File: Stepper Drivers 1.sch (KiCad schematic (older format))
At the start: 88 parts, among them J3 Conn_01x04, J4 Conn_01x04, J5 Conn_01x04, J6 Conn_01x04

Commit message: associated more footprints
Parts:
- C102, C103, C104, C105, C106, C107, C108, C109, C59, C61, C74, C75, C76, C77, C78, C79, C80, C81, C87, C89: footprint (none) -> Capacitor_SMD:C_0603_1608Metric_Pad1.05x0.95mm_HandSolder
- C56, C57, C84, C85: footprint (none) -> Capacitor_SMD:C_0805_2012Metric_Pad1.15x1.40mm_HandSolder
- J3, J4, J5, J6: footprint (none) -> Connector_Molex:Molex_KK-254_AE-6410-04A_1x04_P2.54mm_Vertical
- JP10, JP11, JP6, JP7: footprint (none) -> Connector_PinHeader_2.54mm:PinHeader_1x03_P2.54mm_Vertical
- JP4, JP5, JP8, JP9: footprint (none) -> Connector_PinHeader_2.54mm:PinHeader_1x02_P2.54mm_Vertical
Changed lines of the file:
@@
 F 0 "C61" V 3542 1696 39  0000 L BNN
 F 1 "22nF" V 3542 1605 39  0000 R BNN
-F 2 "" H 3450 1650 50  0001 C CNN
+F 2 "Capacitor_SMD:C_0603_1608Metric_Pad1.05x0.95mm_HandSolder" H 3450 1650 50  0001 C CNN
 F 3 "~" H 3450 1650 50  0001 C CNN
 	1    3450 1650
@@
 F 0 "C57" V 1942 1346 39  0000 L BNN
 F 1 "4.7uF" V 1942 1255 39  0000 R BNN
-F 2 "" H 1850 1300 50  0001 C CNN
+F 2 "Capacitor_SMD:C_0805_2012Metric_Pad1.15x1.40mm_HandSolder" H 1850 1300 50  0001 C CNN
 F 3 "~" H 1850 1300 50  0001 C CNN
 	1    1850 1300
@@
 F 0 "JP5" H 1550 1850 39  0000 R BNN
 F 1 "Stall Detection" H 1650 1900 39  0000 L TNN
-F 2 "" H 1600 1800 50  0001 C CNN
+F 2 "Connector_PinHeader_2.54mm:PinHeader_1x02_P2.54mm_Vertical" H 1600 1800 50  0001 C CNN
 F 3 "~" H 1600 1800 50  0001 C CNN
 	1    1600 1800
@@
 F 0 "C75" V 4542 2296 39  0000 L BNN
 F 1 "1nF" V 4542 2205 39  0000 R BNN
-F 2 "" H 4450 2250 50  0001 C CNN
+F 2 "Capacitor_SMD:C_0603_1608Metric_Pad1.05x0.95mm_HandSolder" H 4450 2250 50  0001 C CNN
 F 3 "~" H 4450 2250 50  0001 C CNN
 	1    4450 2250
@@
 F 0 "C77" V 4692 2296 39  0000 L BNN
 F 1 "1nF" V 4692 2205 39  0000 R BNN
-F 2 "" H 4600 2250 50  0001 C CNN
+F 2 "Capacitor_SMD:C_0603_1608Metric_Pad1.05x0.95mm_HandSolder" H 4600 2250 50  0001 C CNN
 F 3 "~" H 4600 2250 50  0001 C CNN
 	1    4600 2250
@@
 F 0 "C79" V 4842 2296 39  0000 L BNN
 F 1 "1nF" V 4842 2205 39  0000 R BNN
-F 2 "" H 4750 2250 50  0001 C CNN
+F 2 "Capacitor_SMD:C_0603_1608Metric_Pad1.05x0.95mm_HandSolder" H 4750 2250 50  0001 C CNN
 F 3 "~" H 4750 2250 50  0001 C CNN
 	1    4750 2250
@@
 F 0 "C81" V 4992 2296 39  0000 L BNN
 F 1 "1nF" V 4992 2205 39  0000 R BNN
-F 2 "" H 4900 2250 50  0001 C CNN
+F 2 "Capacitor_SMD:C_0603_1608Metric_Pad1.05x0.95mm_HandSolder" H 4900 2250 50  0001 C CNN
 F 3 "~" H 4900 2250 50  0001 C CNN
 	1    4900 2250
@@
 F 0 "J4" H 5280 1292 50  0000 L CNN
 F 1 "Conn_01x04" H 5280 1201 50  0000 L CNN
-F 2 "" H 5200 1300 50  0001 C CNN
+F 2 "Connector_Molex:Molex_KK-254_AE-6410-04A_1x04_P2.54mm_Vertical" H 5200 1300 50  0001 C CNN
 F 3 "~" H 5200 1300 50  0001 C CNN
 	1    5200 1300
@@
 F 0 "C87" V 8892 1696 39  0000 L BNN
 F 1 "22nF" V 8892 1605 39  0000 R BNN
-F 2 "" H 8800 1650 50  0001 C CNN
+F 2 "Capacitor_SMD:C_0603_1608Metric_Pad1.05x0.95mm_HandSolder" H 8800 1650 50  0001 C CNN
 F 3 "~" H 8800 1650 50  0001 C CNN
 	1    8800 1650
@@
 F 0 "C84" V 7292 1346 39  0000 L BNN
 F 1 "4.7uF" V 7292 1255 39  0000 R BNN
-F 2 "" H 7200 1300 50  0001 C CNN
+F 2 "Capacitor_SMD:C_0805_2012Metric_Pad1.15x1.40mm_HandSolder" H 7200 1300 50  0001 C CNN
 F 3 "~" H 7200 1300 50  0001 C CNN
 	1    7200 1300
@@
 F 0 "JP8" H 6900 1850 39  0000 R BNN
 F 1 "Stall Detection" H 7000 1900 39  0000 L TNN
-F 2 "" H 6950 1800 50  0001 C CNN
+F 2 "Connector_PinHeader_2.54mm:PinHeader_1x02_P2.54mm_Vertical" H 6950 1800 50  0001 C CNN
 F 3 "~" H 6950 1800 50  0001 C CNN
 	1    6950 1800
@@
 F 0 "C102" V 9892 2296 39  0000 L BNN
 F 1 "1nF" V 9892 2205 39  0000 R BNN
-F 2 "" H 9800 2250 50  0001 C CNN
+F 2 "Capacitor_SMD:C_0603_1608Metric_Pad1.05x0.95mm_HandSolder" H 9800 2250 50  0001 C CNN
 F 3 "~" H 9800 2250 50  0001 C CNN
 	1    9800 2250
@@
 F 0 "C104" V 10042 2296 39  0000 L BNN
 F 1 "1nF" V 10042 2205 39  0000 R BNN
-F 2 "" H 9950 2250 50  0001 C CNN
+F 2 "Capacitor_SMD:C_0603_1608Metric_Pad1.05x0.95mm_HandSolder" H 9950 2250 50  0001 C CNN
 F 3 "~" H 9950 2250 50  0001 C CNN
 	1    9950 2250
@@
 F 0 "C106" V 10192 2296 39  0000 L BNN
 F 1 "1nF" V 10192 2205 39  0000 R BNN
-F 2 "" H 10100 2250 50  0001 C CNN
+F 2 "Capacitor_SMD:C_0603_1608Metric_Pad1.05x0.95mm_HandSolder" H 10100 2250 50  0001 C CNN
 F 3 "~" H 10100 2250 50  0001 C CNN
 	1    10100 2250
@@
 F 0 "C108" V 10342 2296 39  0000 L BNN
 F 1 "1nF" V 10342 2205 39  0000 R BNN
-F 2 "" H 10250 2250 50  0001 C CNN
+F 2 "Capacitor_SMD:C_0603_1608Metric_Pad1.05x0.95mm_HandSolder" H 10250 2250 50  0001 C CNN
 F 3 "~" H 10250 2250 50  0001 C CNN
 	1    10250 2250
@@
 F 0 "J5" H 10630 1292 50  0000 L CNN
 F 1 "Conn_01x04" H 10630 1201 50  0000 L CNN
-F 2 "" H 10550 1300 50  0001 C CNN
+F 2 "Connector_Molex:Molex_KK-254_AE-6410-04A_1x04_P2.54mm_Vertical" H 10550 1300 50  0001 C CNN
 F 3 "~" H 10550 1300 50  0001 C CNN
 	1    10550 1300
@@
 F 0 "C59" V 3492 4646 39  0000 L BNN
 F 1 "22nF" V 3492 4555 39  0000 R BNN
-F 2 "" H 3400 4600 50  0001 C CNN
+F 2 "Capacitor_SMD:C_0603_1608Metric_Pad1.05x0.95mm_HandSolder" H 3400 4600 50  0001 C CNN
 F 3 "~" H 3400 4600 50  0001 C CNN
 	1    3400 4600
@@
 F 0 "C56" V 1892 4296 39  0000 L BNN
 F 1 "4.7uF" V 1892 4205 39  0000 R BNN
-F 2 "" H 1800 4250 50  0001 C CNN
+F 2 "Capacitor_SMD:C_0805_2012Metric_Pad1.15x1.40mm_HandSolder" H 1800 4250 50  0001 C CNN
 F 3 "~" H 1800 4250 50  0001 C CNN
 	1    1800 4250
@@
 F 0 "JP4" H 1500 4800 39  0000 R BNN
 F 1 "Stall Detection" H 1600 4850 39  0000 L TNN
-F 2 "" H 1550 4750 50  0001 C CNN
+F 2 "Connector_PinHeader_2.54mm:PinHeader_1x02_P2.54mm_Vertical" H 1550 4750 50  0001 C CNN
 F 3 "~" H 1550 4750 50  0001 C CNN
 	1    1550 4750
@@
 F 0 "C74" V 4492 5246 39  0000 L BNN
 F 1 "1nF" V 4492 5155 39  0000 R BNN
-F 2 "" H 4400 5200 50  0001 C CNN
+F 2 "Capacitor_SMD:C_0603_1608Metric_Pad1.05x0.95mm_HandSolder" H 4400 5200 50  0001 C CNN
 F 3 "~" H 4400 5200 50  0001 C CNN
 	1    4400 5200
@@
 F 0 "C76" V 4642 5246 39  0000 L BNN
 F 1 "1nF" V 4642 5155 39  0000 R BNN
-F 2 "" H 4550 5200 50  0001 C CNN
+F 2 "Capacitor_SMD:C_0603_1608Metric_Pad1.05x0.95mm_HandSolder" H 4550 5200 50  0001 C CNN
 F 3 "~" H 4550 5200 50  0001 C CNN
 	1    4550 5200
@@
 F 0 "C78" V 4792 5246 39  0000 L BNN
 F 1 "1nF" V 4792 5155 39  0000 R BNN
-F 2 "" H 4700 5200 50  0001 C CNN
+F 2 "Capacitor_SMD:C_0603_1608Metric_Pad1.05x0.95mm_HandSolder" H 4700 5200 50  0001 C CNN
 F 3 "~" H 4700 5200 50  0001 C CNN
 	1    4700 5200
@@
 F 0 "C80" V 4942 5246 39  0000 L BNN
 F 1 "1nF" V 4942 5155 39  0000 R BNN
-F 2 "" H 4850 5200 50  0001 C CNN
+F 2 "Capacitor_SMD:C_0603_1608Metric_Pad1.05x0.95mm_HandSolder" H 4850 5200 50  0001 C CNN
 F 3 "~" H 4850 5200 50  0001 C CNN
 	1    4850 5200
@@
 F 0 "J3" H 5230 4242 50  0000 L CNN
 F 1 "Conn_01x04" H 5230 4151 50  0000 L CNN
-F 2 "" H 5150 4250 50  0001 C CNN
+F 2 "Connector_Molex:Molex_KK-254_AE-6410-04A_1x04_P2.54mm_Vertical" H 5150 4250 50  0001 C CNN
 F 3 "~" H 5150 4250 50  0001 C CNN
 	1    5150 4250
@@
 F 0 "C89" V 8892 4646 39  0000 L BNN
 F 1 "22nF" V 8892 4555 39  0000 R BNN
-F 2 "" H 8800 4600 50  0001 C CNN
+F 2 "Capacitor_SMD:C_0603_1608Metric_Pad1.05x0.95mm_HandSolder" H 8800 4600 50  0001 C CNN
 F 3 "~" H 8800 4600 50  0001 C CNN
 	1    8800 4600
@@
 F 0 "C85" V 7292 4296 39  0000 L BNN
 F 1 "4.7uF" V 7292 4205 39  0000 R BNN
-F 2 "" H 7200 4250 50  0001 C CNN
+F 2 "Capacitor_SMD:C_0805_2012Metric_Pad1.15x1.40mm_HandSolder" H 7200 4250 50  0001 C CNN
 F 3 "~" H 7200 4250 50  0001 C CNN
 	1    7200 4250
@@
 F 0 "JP9" H 6900 4800 39  0000 R BNN
 F 1 "Stall Detection" H 7000 4850 39  0000 L TNN
-F 2 "" H 6950 4750 50  0001 C CNN
+F 2 "Connector_PinHeader_2.54mm:PinHeader_1x02_P2.54mm_Vertical" H 6950 4750 50  0001 C CNN
 F 3 "~" H 6950 4750 50  0001 C CNN
 	1    6950 4750
@@
 F 0 "C103" V 9892 5246 39  0000 L BNN
 F 1 "1nF" V 9892 5155 39  0000 R BNN
-F 2 "" H 9800 5200 50  0001 C CNN
+F 2 "Capacitor_SMD:C_0603_1608Metric_Pad1.05x0.95mm_HandSolder" H 9800 5200 50  0001 C CNN
 F 3 "~" H 9800 5200 50  0001 C CNN
 	1    9800 5200
@@
 F 0 "C105" V 10042 5246 39  0000 L BNN
 F 1 "1nF" V 10042 5155 39  0000 R BNN
-F 2 "" H 9950 5200 50  0001 C CNN
+F 2 "Capacitor_SMD:C_0603_1608Metric_Pad1.05x0.95mm_HandSolder" H 9950 5200 50  0001 C CNN
 F 3 "~" H 9950 5200 50  0001 C CNN
 	1    9950 5200
@@
 F 0 "C107" V 10192 5246 39  0000 L BNN
 F 1 "1nF" V 10192 5155 39  0000 R BNN
-F 2 "" H 10100 5200 50  0001 C CNN
+F 2 "Capacitor_SMD:C_0603_1608Metric_Pad1.05x0.95mm_HandSolder" H 10100 5200 50  0001 C CNN
 F 3 "~" H 10100 5200 50  0001 C CNN
 	1    10100 5200
@@
 F 0 "C109" V 10342 5246 39  0000 L BNN
 F 1 "1nF" V 10342 5155 39  0000 R BNN
-F 2 "" H 10250 5200 50  0001 C CNN
+F 2 "Capacitor_SMD:C_0603_1608Metric_Pad1.05x0.95mm_HandSolder" H 10250 5200 50  0001 C CNN
 F 3 "~" H 10250 5200 50  0001 C CNN
 	1    10250 5200
@@
 F 0 "J6" H 10630 4242 50  0000 L CNN
 F 1 "Conn_01x04" H 10630 4151 50  0000 L CNN
-F 2 "" H 10550 4250 50  0001 C CNN
+F 2 "Connector_Molex:Molex_KK-254_AE-6410-04A_1x04_P2.54mm_Vertical" H 10550 4250 50  0001 C CNN
 F 3 "~" H 10550 4250 50  0001 C CNN
 	1    10550 4250
@@
 F 0 "JP7" H 3300 3063 50  0000 C CNN
 F 1 "SPREAD_STEALTH" H 3150 3150 50  0000 C CNN
-F 2 "" H 3300 2950 50  0001 C CNN
+F 2 "Connector_PinHeader_2.54mm:PinHeader_1x03_P2.54mm_Vertical" H 3300 2950 50  0001 C CNN
 F 3 "~" H 3300 2950 50  0001 C CNN
 	1    3300 2950
@@
 F 0 "JP6" H 3250 6013 50  0000 C CNN
 F 1 "SPREAD_STEALTH" H 3100 6100 50  0000 C CNN
-F 2 "" H 3250 5900 50  0001 C CNN
+F 2 "Connector_PinHeader_2.54mm:PinHeader_1x03_P2.54mm_Vertical" H 3250 5900 50  0001 C CNN
 F 3 "~" H 3250 5900 50  0001 C CNN
 	1    3250 5900
@@
 F 0 "JP10" H 8650 3063 50  0000 C CNN
 F 1 "SPREAD_STEALTH" H 8500 3150 50  0000 C CNN
-F 2 "" H 8650 2950 50  0001 C CNN
+F 2 "Connector_PinHeader_2.54mm:PinHeader_1x03_P2.54mm_Vertical" H 8650 2950 50  0001 C CNN
 F 3 "~" H 8650 2950 50  0001 C CNN
 	1    8650 2950
@@
 F 0 "JP11" H 8650 6013 50  0000 C CNN
 F 1 "SPREAD_STEALTH" H 8500 6100 50  0000 C CNN
-F 2 "" H 8650 5900 50  0001 C CNN
+F 2 "Connector_PinHeader_2.54mm:PinHeader_1x03_P2.54mm_Vertical" H 8650 5900 50  0001 C CNN
 F 3 "~" H 8650 5900 50  0001 C CNN
 	1    8650 5900

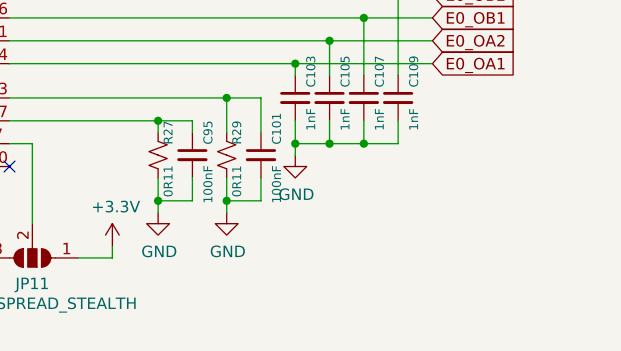
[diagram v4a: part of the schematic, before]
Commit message: Added more footprints
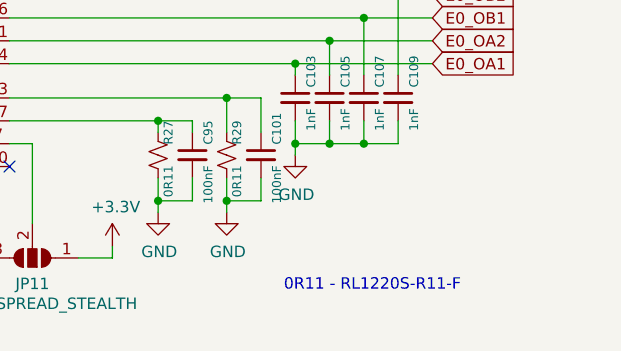
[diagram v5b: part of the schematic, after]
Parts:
- E0_Driver1, X_Driver1, Y_Driver1, Z_Driver1: footprint (none) -> Package_DFN_QFN:QFN-28-1EP_5x5mm_P0.5mm_EP3.35x3.35mm_ThermalVias
- R14, R15, R22, R23: footprint (none) -> Resistor_SMD:R_0603_1608Metric_Pad1.05x0.95mm_HandSolder
- R16, R17, R18, R19, R20, R21, R24, R25, R26, R27, R28, R29: footprint (none) -> Resistor_SMD:R_0805_2012Metric_Pad1.15x1.40mm_HandSolder
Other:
- note added: "0R11 - RL1220S-R11-F"
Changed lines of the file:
@@
 $Descr A4 11693 8268
 encoding utf-8
-Sheet 3 9
+Sheet 9 9
 Title ""
 Date "2020-10-23"
@@
 F 0 "X_Driver1" H 2600 2565 50  0000 C CNN
 F 1 "TMC2209" H 2600 2474 50  0000 C CNN
-F 2 "" H 2700 1750 50  0001 C CNN
+F 2 "Package_DFN_QFN:QFN-28-1EP_5x5mm_P0.5mm_EP3.35x3.35mm_ThermalVias" H 2700 1750 50  0001 C CNN
 F 3 "" H 2700 1750 50  0001 C CNN
 	1    2600 1750
@@
 F 0 "R19" V 3918 2546 39  0000 L BNN
 F 1 "0R11" V 3918 2455 39  0000 R BNN
-F 2 "" H 3850 2500 50  0001 C CNN
+F 2 "Resistor_SMD:R_0805_2012Metric_Pad1.15x1.40mm_HandSolder" H 3850 2500 50  0001 C CNN
 F 3 "~" H 3850 2500 50  0001 C CNN
 	1    3850 2500
@@
 F 0 "R21" V 4218 2546 39  0000 L BNN
 F 1 "0R11" V 4218 2455 39  0000 R BNN
-F 2 "" H 4150 2500 50  0001 C CNN
+F 2 "Resistor_SMD:R_0805_2012Metric_Pad1.15x1.40mm_HandSolder" H 4150 2500 50  0001 C CNN
 F 3 "~" H 4150 2500 50  0001 C CNN
 	1    4150 2500
@@
 F 0 "R17" V 1368 2346 39  0000 L BNN
 F 1 "0R11" V 1368 2255 39  0000 R BNN
-F 2 "" H 1300 2300 50  0001 C CNN
+F 2 "Resistor_SMD:R_0805_2012Metric_Pad1.15x1.40mm_HandSolder" H 1300 2300 50  0001 C CNN
 F 3 "~" H 1300 2300 50  0001 C CNN
 	1    1300 2300
@@
 F 0 "R15" V 1168 1396 39  0000 L BNN
 F 1 "20k" V 1168 1305 39  0000 R BNN
-F 2 "" H 1100 1350 50  0001 C CNN
+F 2 "Resistor_SMD:R_0603_1608Metric_Pad1.05x0.95mm_HandSolder" H 1100 1350 50  0001 C CNN
 F 3 "~" H 1100 1350 50  0001 C CNN
 	1    1100 1350
@@
 F 0 "Y_Driver1" H 7950 2565 50  0000 C CNN
 F 1 "TMC2209" H 7950 2474 50  0000 C CNN
-F 2 "" H 8050 1750 50  0001 C CNN
+F 2 "Package_DFN_QFN:QFN-28-1EP_5x5mm_P0.5mm_EP3.35x3.35mm_ThermalVias" H 8050 1750 50  0001 C CNN
 F 3 "" H 8050 1750 50  0001 C CNN
 	1    7950 1750
@@
 F 0 "R26" V 9268 2546 39  0000 L BNN
 F 1 "0R11" V 9268 2455 39  0000 R BNN
-F 2 "" H 9200 2500 50  0001 C CNN
+F 2 "Resistor_SMD:R_0805_2012Metric_Pad1.15x1.40mm_HandSolder" H 9200 2500 50  0001 C CNN
 F 3 "~" H 9200 2500 50  0001 C CNN
 	1    9200 2500
@@
 F 0 "R28" V 9568 2546 39  0000 L BNN
 F 1 "0R11" V 9568 2455 39  0000 R BNN
-F 2 "" H 9500 2500 50  0001 C CNN
+F 2 "Resistor_SMD:R_0805_2012Metric_Pad1.15x1.40mm_HandSolder" H 9500 2500 50  0001 C CNN
 F 3 "~" H 9500 2500 50  0001 C CNN
 	1    9500 2500
@@
 F 0 "R24" V 6718 2346 39  0000 L BNN
 F 1 "0R11" V 6718 2255 39  0000 R BNN
-F 2 "" H 6650 2300 50  0001 C CNN
+F 2 "Resistor_SMD:R_0805_2012Metric_Pad1.15x1.40mm_HandSolder" H 6650 2300 50  0001 C CNN
 F 3 "~" H 6650 2300 50  0001 C CNN
 	1    6650 2300
@@
 F 0 "R22" V 6518 1396 39  0000 L BNN
 F 1 "20k" V 6518 1305 39  0000 R BNN
-F 2 "" H 6450 1350 50  0001 C CNN
+F 2 "Resistor_SMD:R_0603_1608Metric_Pad1.05x0.95mm_HandSolder" H 6450 1350 50  0001 C CNN
 F 3 "~" H 6450 1350 50  0001 C CNN
 	1    6450 1350
@@
 F 0 "Z_Driver1" H 2550 5515 50  0000 C CNN
 F 1 "TMC2209" H 2550 5424 50  0000 C CNN
-F 2 "" H 2650 4700 50  0001 C CNN
+F 2 "Package_DFN_QFN:QFN-28-1EP_5x5mm_P0.5mm_EP3.35x3.35mm_ThermalVias" H 2650 4700 50  0001 C CNN
 F 3 "" H 2650 4700 50  0001 C CNN
 	1    2550 4700
@@
 F 0 "R18" V 3868 5496 39  0000 L BNN
 F 1 "0R11" V 3868 5405 39  0000 R BNN
-F 2 "" H 3800 5450 50  0001 C CNN
+F 2 "Resistor_SMD:R_0805_2012Metric_Pad1.15x1.40mm_HandSolder" H 3800 5450 50  0001 C CNN
 F 3 "~" H 3800 5450 50  0001 C CNN
 	1    3800 5450
@@
 F 0 "R20" V 4168 5496 39  0000 L BNN
 F 1 "0R11" V 4168 5405 39  0000 R BNN
-F 2 "" H 4100 5450 50  0001 C CNN
+F 2 "Resistor_SMD:R_0805_2012Metric_Pad1.15x1.40mm_HandSolder" H 4100 5450 50  0001 C CNN
 F 3 "~" H 4100 5450 50  0001 C CNN
 	1    4100 5450
@@
 F 0 "R16" V 1318 5296 39  0000 L BNN
 F 1 "0R11" V 1318 5205 39  0000 R BNN
-F 2 "" H 1250 5250 50  0001 C CNN
+F 2 "Resistor_SMD:R_0805_2012Metric_Pad1.15x1.40mm_HandSolder" H 1250 5250 50  0001 C CNN
 F 3 "~" H 1250 5250 50  0001 C CNN
 	1    1250 5250
@@
 F 0 "R14" V 1118 4346 39  0000 L BNN
 F 1 "20k" V 1118 4255 39  0000 R BNN
-F 2 "" H 1050 4300 50  0001 C CNN
+F 2 "Resistor_SMD:R_0603_1608Metric_Pad1.05x0.95mm_HandSolder" H 1050 4300 50  0001 C CNN
 F 3 "~" H 1050 4300 50  0001 C CNN
 	1    1050 4300
@@
 F 0 "R27" V 9268 5496 39  0000 L BNN
 F 1 "0R11" V 9268 5405 39  0000 R BNN
-F 2 "" H 9200 5450 50  0001 C CNN
+F 2 "Resistor_SMD:R_0805_2012Metric_Pad1.15x1.40mm_HandSolder" H 9200 5450 50  0001 C CNN
 F 3 "~" H 9200 5450 50  0001 C CNN
 	1    9200 5450
@@
 F 0 "R29" V 9568 5496 39  0000 L BNN
 F 1 "0R11" V 9568 5405 39  0000 R BNN
-F 2 "" H 9500 5450 50  0001 C CNN
+F 2 "Resistor_SMD:R_0805_2012Metric_Pad1.15x1.40mm_HandSolder" H 9500 5450 50  0001 C CNN
 F 3 "~" H 9500 5450 50  0001 C CNN
 	1    9500 5450
@@
 F 0 "R25" V 6718 5296 39  0000 L BNN
 F 1 "0R11" V 6718 5205 39  0000 R BNN
-F 2 "" H 6650 5250 50  0001 C CNN
+F 2 "Resistor_SMD:R_0805_2012Metric_Pad1.15x1.40mm_HandSolder" H 6650 5250 50  0001 C CNN
 F 3 "~" H 6650 5250 50  0001 C CNN
 	1    6650 5250
@@
 F 0 "R23" V 6518 4346 39  0000 L BNN
 F 1 "20k" V 6518 4255 39  0000 R BNN
-F 2 "" H 6450 4300 50  0001 C CNN
+F 2 "Resistor_SMD:R_0603_1608Metric_Pad1.05x0.95mm_HandSolder" H 6450 4300 50  0001 C CNN
 F 3 "~" H 6450 4300 50  0001 C CNN
 	1    6450 4300
@@
 F 0 "E0_Driver1" H 7950 5515 50  0000 C CNN
 F 1 "TMC2209" H 7950 5424 50  0000 C CNN
-F 2 "" H 8050 4700 50  0001 C CNN
+F 2 "Package_DFN_QFN:QFN-28-1EP_5x5mm_P0.5mm_EP3.35x3.35mm_ThermalVias" H 8050 4700 50  0001 C CNN
 F 3 "" H 8050 4700 50  0001 C CNN
 	1    7950 4700
@@
 Wire Wire Line
 	7050 4750 7350 4750
+Text Notes 9750 6050 0    50   ~ 0
+0R11 - RL1220S-R11-F
 $EndSCHEMATC

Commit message: started some routing
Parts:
- JP10, JP11, JP6, JP7: footprint Connector_PinHeader_2.54mm:PinHeader_1x03_P2.54mm_Vertical -> Jumper:SolderJumper-3_P1.3mm_Open_RoundedPad1.0x1.5mm
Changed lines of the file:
@@
 F 0 "JP7" H 3300 3063 50  0000 C CNN
 F 1 "SPREAD_STEALTH" H 3150 3150 50  0000 C CNN
-F 2 "Connector_PinHeader_2.54mm:PinHeader_1x03_P2.54mm_Vertical" H 3300 2950 50  0001 C CNN
+F 2 "Jumper:SolderJumper-3_P1.3mm_Open_RoundedPad1.0x1.5mm" H 3300 2950 50  0001 C CNN
 F 3 "~" H 3300 2950 50  0001 C CNN
 	1    3300 2950
@@
 F 0 "JP6" H 3250 6013 50  0000 C CNN
 F 1 "SPREAD_STEALTH" H 3100 6100 50  0000 C CNN
-F 2 "Connector_PinHeader_2.54mm:PinHeader_1x03_P2.54mm_Vertical" H 3250 5900 50  0001 C CNN
+F 2 "Jumper:SolderJumper-3_P1.3mm_Open_RoundedPad1.0x1.5mm" H 3250 5900 50  0001 C CNN
 F 3 "~" H 3250 5900 50  0001 C CNN
 	1    3250 5900
@@
 F 0 "JP10" H 8650 3063 50  0000 C CNN
 F 1 "SPREAD_STEALTH" H 8500 3150 50  0000 C CNN
-F 2 "Connector_PinHeader_2.54mm:PinHeader_1x03_P2.54mm_Vertical" H 8650 2950 50  0001 C CNN
+F 2 "Jumper:SolderJumper-3_P1.3mm_Open_RoundedPad1.0x1.5mm" H 8650 2950 50  0001 C CNN
 F 3 "~" H 8650 2950 50  0001 C CNN
 	1    8650 2950
@@
 F 0 "JP11" H 8650 6013 50  0000 C CNN
 F 1 "SPREAD_STEALTH" H 8500 6100 50  0000 C CNN
-F 2 "Connector_PinHeader_2.54mm:PinHeader_1x03_P2.54mm_Vertical" H 8650 5900 50  0001 C CNN
+F 2 "Jumper:SolderJumper-3_P1.3mm_Open_RoundedPad1.0x1.5mm" H 8650 5900 50  0001 C CNN
 F 3 "~" H 8650 5900 50  0001 C CNN
 	1    8650 5900
